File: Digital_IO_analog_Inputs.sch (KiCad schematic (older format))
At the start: 33 parts, among them J5 OSTTC020162, J7 OSTTC030162, J9 0022232031, Q3 BC817-25LT1G, Q4 BC817-25LT1G, U17 ISO1211DR, U24 ISO1211DR, U26 ISO1211DR

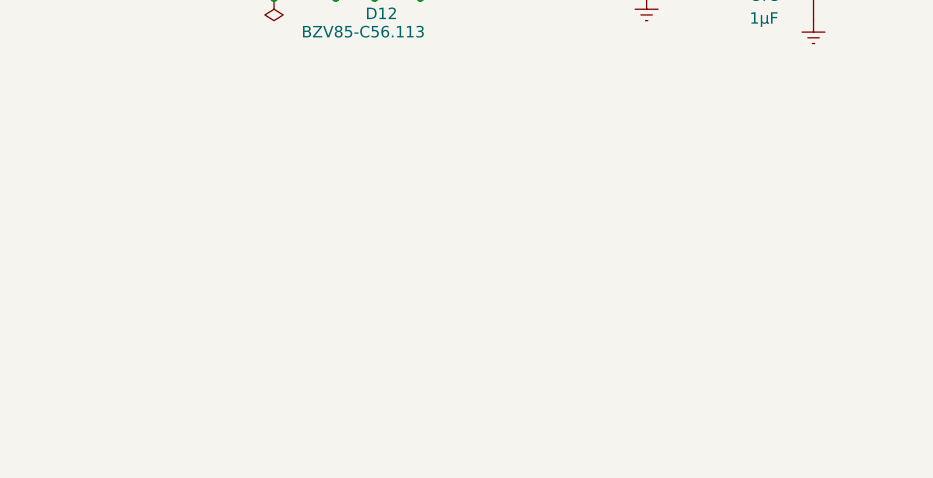
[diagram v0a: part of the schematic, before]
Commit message: Analog decoupling schema completed. Digital_IO completed and clean up
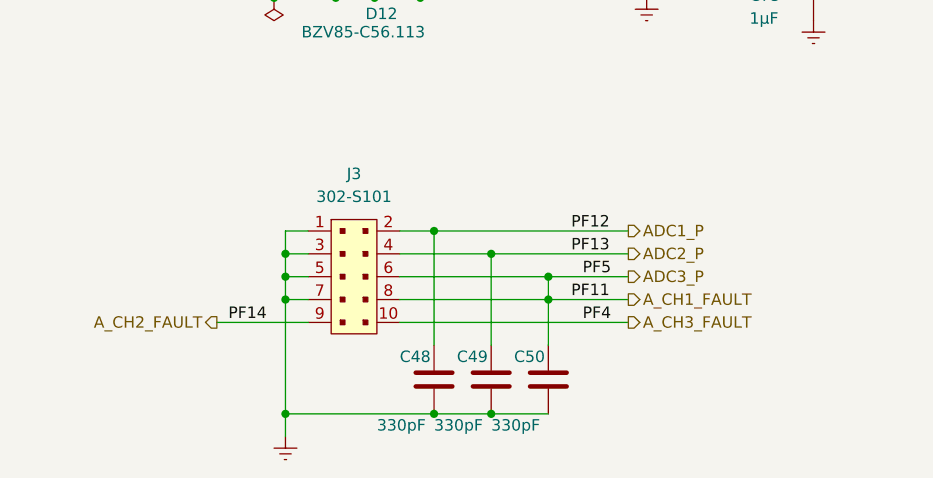
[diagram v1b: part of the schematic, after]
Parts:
- added C48, C49, C50: 330pF, Capacitor_SMD:C_0603_1608Metric_Pad1.08x0.95mm_HandSolder, symbol Device:C
- added J3: 302-S101, digikey-footprints:PinHeader_2x5_P2.54mm_Drill1.2mm, symbol dk_Rectangular-Connectors-Headers-Male-Pins:302-S101
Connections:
- net GNDREF: now also C48.2, C49.2, C50.2, J3.1, J3.3, J3.5, J3.7
- new net ADC1_P: C48.1, J3.2
- new net ADC2_P: C49.1, J3.4
- new net ADC3_P: C50.1, J3.6, J3.8
- new net A_CH2_FAULT: J3.9
- new net A_CH3_FAULT: J3.10
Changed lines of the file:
@@
 Wire Wire Line
 	7920 4280 7920 4410
+Text HLabel 3350 5450 2    50   Output ~ 0
+ADC1_P
+Text HLabel 3350 5750 2    50   Output ~ 0
+A_CH1_FAULT
+Text HLabel 3350 5550 2    50   Output ~ 0
+ADC2_P
+Text HLabel 1550 5850 0    50   Output ~ 0
+A_CH2_FAULT
+Text HLabel 3350 5650 2    50   Output ~ 0
+ADC3_P
+Text HLabel 3350 5850 2    50   Output ~ 0
+A_CH3_FAULT
+$Comp
+L dk_Rectangular-Connectors-Headers-Male-Pins:302-S101 J3
+U 1 1 60B0C96F
+P 2150 5650
+F 0 "J3" H 2150 6100 50  0000 C CNN
+F 1 "302-S101" H 2150 6000 50  0000 C CNN
+F 2 "digikey-footprints:PinHeader_2x5_P2.54mm_Drill1.2mm" H 2350 5850 60  0001 L CNN
+F 3 "http://www.on-shore.com/wp-content/uploads/2018/04/302-SXX1.pdf" V 2350 5950 60  0001 L CNN
+F 4 "ED1543-ND" H 2350 6050 60  0001 L CNN "Digi-Key_PN"
+F 5 "302-S101" H 2350 6150 60  0001 L CNN "MPN"
+F 6 "Connectors, Interconnects" H 2350 6250 60  0001 L CNN "Category"
+F 7 "Rectangular Connectors - Headers, Male Pins" H 2350 6350 60  0001 L CNN "Family"
+F 8 "http://www.on-shore.com/wp-content/uploads/2018/04/302-SXX1.pdf" H 2350 6450 60  0001 L CNN "DK_Datasheet_Link"
+F 9 "/product-detail/en/on-shore-technology-inc/302-S101/ED1543-ND/2178422" H 2350 6550 60  0001 L CNN "DK_Detail_Page"
+F 10 "CONN HEADER VERT 10POS 2.54MM" H 2350 6650 60  0001 L CNN "Description"
+F 11 "On Shore Technology Inc." H 2350 6750 60  0001 L CNN "Manufacturer"
+F 12 "Active" H 2350 6850 60  0001 L CNN "Status"
+	1    2150 5650
+	1    0    0    -1
+$EndComp
+Wire Wire Line
+	1950 5850 1550 5850
+Wire Wire Line
+	2350 5450 2500 5450
+Wire Wire Line
+	1950 5450 1850 5450
+Wire Wire Line
+	1850 5450 1850 5550
+Wire Wire Line
+	1950 5550 1850 5550
+Connection ~ 1850 5550
+Wire Wire Line
+	1850 5550 1850 5650
+Wire Wire Line
+	1950 5650 1850 5650
+Connection ~ 1850 5650
+Wire Wire Line
+	1850 5650 1850 5750
+Wire Wire Line
+	1950 5750 1850 5750
+Connection ~ 1850 5750
+Wire Wire Line
+	1850 5750 1850 6250
+$Comp
+L Device:C C?
+U 1 1 60B910A1
+P 2500 6100
+AR Path="/60B910A1" Ref="C?"  Part="1"
+AR Path="/60A03F8A/60B910A1" Ref="C?"  Part="1"
+AR Path="/60D8C564/60B910A1" Ref="C48"  Part="1"
+F 0 "C48" H 2350 6200 50  0000 L CNN
+F 1 "330pF" H 2250 5900 50  0000 L CNN
+F 2 "Capacitor_SMD:C_0603_1608Metric_Pad1.08x0.95mm_HandSolder" H 2538 5950 50  0001 C CNN
+F 3 "http://www.farnell.com/datasheets/2710676.pdf" H 2500 6100 50  0001 C CNN
+F 4 "GRM188R71H331KA01D" H 2500 6100 50  0001 C CNN "Type"
+	1    2500 6100
+	1    0    0    -1
+$EndComp
+Wire Wire Line
+	2500 5950 2500 5450
+$Comp
+L Device:C C?
+U 1 1 60B9DA68
+P 2750 6100
+AR Path="/60B9DA68" Ref="C?"  Part="1"
+AR Path="/60A03F8A/60B9DA68" Ref="C?"  Part="1"
+AR Path="/60D8C564/60B9DA68" Ref="C49"  Part="1"
+F 0 "C49" H 2600 6200 50  0000 L CNN
+F 1 "330pF" H 2500 5900 50  0000 L CNN
+F 2 "Capacitor_SMD:C_0603_1608Metric_Pad1.08x0.95mm_HandSolder" H 2788 5950 50  0001 C CNN
+F 3 "http://www.farnell.com/datasheets/2710676.pdf" H 2750 6100 50  0001 C CNN
+F 4 "GRM188R71H331KA01D" H 2750 6100 50  0001 C CNN "Type"
+	1    2750 6100
+	1    0    0    -1
+$EndComp
+$Comp
+L Device:C C?
+U 1 1 60B9DF75
+P 3000 6100
+AR Path="/60B9DF75" Ref="C?"  Part="1"
+AR Path="/60A03F8A/60B9DF75" Ref="C?"  Part="1"
+AR Path="/60D8C564/60B9DF75" Ref="C50"  Part="1"
+F 0 "C50" H 2850 6200 50  0000 L CNN
+F 1 "330pF" H 2750 5900 50  0000 L CNN
+F 2 "Capacitor_SMD:C_0603_1608Metric_Pad1.08x0.95mm_HandSolder" H 3038 5950 50  0001 C CNN
+F 3 "http://www.farnell.com/datasheets/2710676.pdf" H 3000 6100 50  0001 C CNN
+F 4 "GRM188R71H331KA01D" H 3000 6100 50  0001 C CNN "Type"
+	1    3000 6100
+	1    0    0    -1
+$EndComp
+Wire Wire Line
+	2750 5950 2750 5550
+Wire Wire Line
+	2750 5550 2350 5550
+Wire Wire Line
+	3000 5950 3000 5750
+Wire Wire Line
+	2350 5650 3000 5650
+Wire Wire Line
+	3000 5650 3350 5650
+Wire Wire Line
+	2350 5750 3000 5750
+Wire Wire Line
+	2350 5850 3350 5850
+Wire Wire Line
+	2750 5550 3350 5550
+Wire Wire Line
+	2500 5450 3350 5450
+$Comp
+L power:GNDREF #PWR?
+U 1 1 60BCDF96
+P 1850 6350
+AR Path="/60BCDF96" Ref="#PWR?"  Part="1"
+AR Path="/60A03F8A/60BCDF96" Ref="#PWR?"  Part="1"
+AR Path="/60D8C564/60BCDF96" Ref="#PWR0103"  Part="1"
+F 0 "#PWR0103" H 1850 6100 50  0001 C CNN
+F 1 "GNDREF" V 1855 6222 50  0001 R CNN
+F 2 "" H 1850 6350 50  0001 C CNN
+F 3 "" H 1850 6350 50  0001 C CNN
+	1    1850 6350
+	1    0    0    -1
+$EndComp
+Wire Wire Line
+	1850 6250 2500 6250
+Connection ~ 1850 6250
+Wire Wire Line
+	1850 6250 1850 6350
+Connection ~ 2500 6250
+Wire Wire Line
+	2500 6250 2750 6250
+Connection ~ 2750 6250
+Wire Wire Line
+	2750 6250 3000 6250
+Text Label 3150 5650 0    50   ~ 0
+PF5
+Text Label 3150 5850 0    50   ~ 0
+PF4
+Text Label 3100 5550 0    50   ~ 0
+PF13
+Text Label 1600 5850 0    50   ~ 0
+PF14
+Text Label 3100 5450 0    50   ~ 0
+PF12
+Text Label 3100 5750 0    50   ~ 0
+PF11
+Connection ~ 3000 5750
+Wire Wire Line
+	3000 5750 3000 5650
+Wire Wire Line
+	3000 5750 3350 5750
+Connection ~ 2500 5450
+Connection ~ 2750 5550
+Connection ~ 3000 5650
 $EndSCHEMATC

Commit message: main PCB changes
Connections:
- net ADC3_P: no longer J3.8
- new net A_CH1_FAULT: J3.8
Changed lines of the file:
@@
 	2750 5550 2350 5550
-Wire Wire Line
-	3000 5950 3000 5750
-Wire Wire Line
-	2350 5650 3000 5650
-Wire Wire Line
-	3000 5650 3350 5650
-Wire Wire Line
-	2350 5750 3000 5750
 Wire Wire Line
 	2350 5850 3350 5850
@@
 Text Label 3100 5750 0    50   ~ 0
 PF11
-Connection ~ 3000 5750
-Wire Wire Line
-	3000 5750 3000 5650
-Wire Wire Line
-	3000 5750 3350 5750
 Connection ~ 2500 5450
 Connection ~ 2750 5550
+Wire Wire Line
+	2350 5650 3000 5650
+Wire Wire Line
+	2350 5750 3350 5750
+Wire Wire Line
+	3000 5650 3000 5950
 Connection ~ 3000 5650
+Wire Wire Line
+	3000 5650 3350 5650
 $EndSCHEMATC

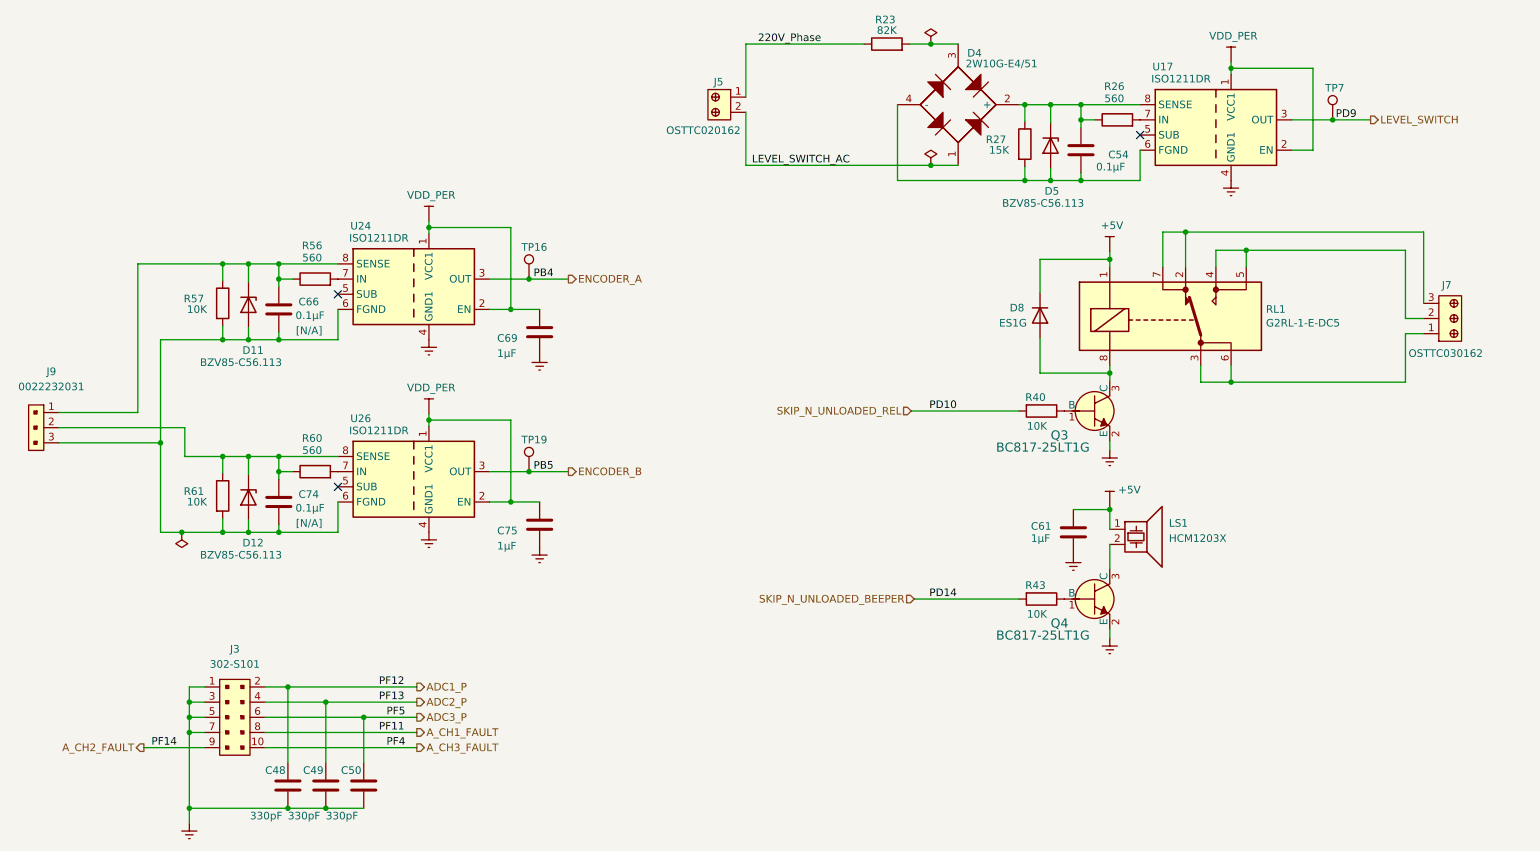
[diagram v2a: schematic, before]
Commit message: LAN elements placed
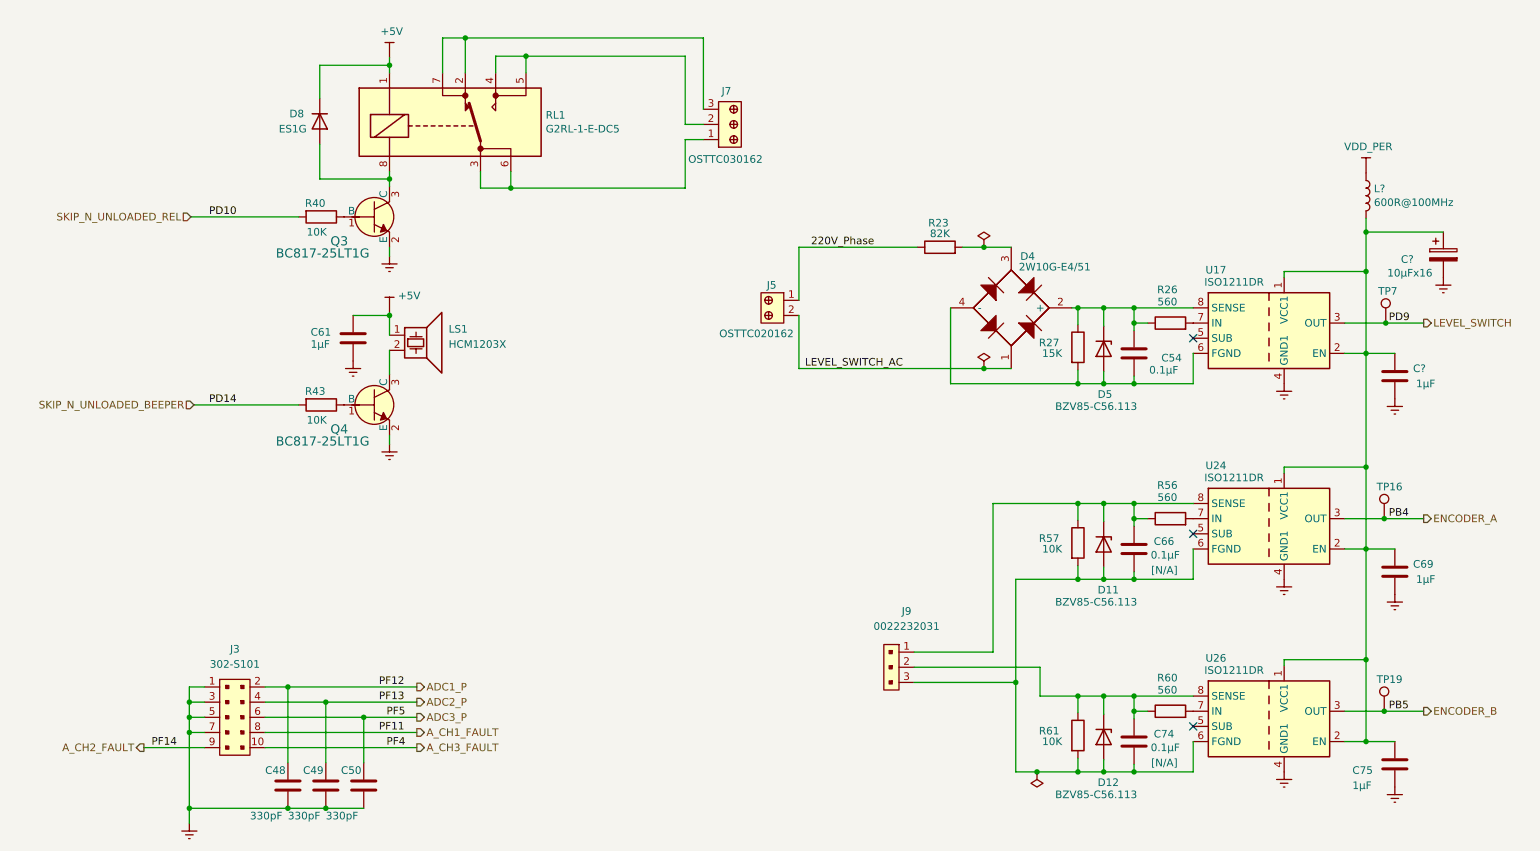
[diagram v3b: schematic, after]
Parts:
- added C?: 1µF, Capacitor_SMD:C_0603_1608Metric_Pad1.08x0.95mm_HandSolder, symbol Device:C
- added C?: 10µFx16, Capacitor_Tantalum_SMD:CP_EIA-3216-10_Kemet-I, symbol Device:CP
- added L?: 600R@100MHz, Inductor_SMD:L_0805_2012Metric_Pad1.15x1.40mm_HandSolder, symbol Device:L
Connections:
- net GNDREF: now also C?.2, C?.2
- net VDD_PER: now also L?.1; no longer C69.1, C75.1, U17.1 (VCC1), U17.2 (EN), U24.1 (VCC1), U24.2 (EN), U26.1 (VCC1), U26.2 (EN)
- new net: C69.1, C75.1, C?.1, C?.1, L?.2, U17.1 (VCC1), U17.2 (EN), U24.1 (VCC1), U24.2 (EN), U26.1 (VCC1), U26.2 (EN)
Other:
- moved on the sheet: C54, C61, C66, C69, C74, C75, D11, D12, D4, D5, D8, J5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

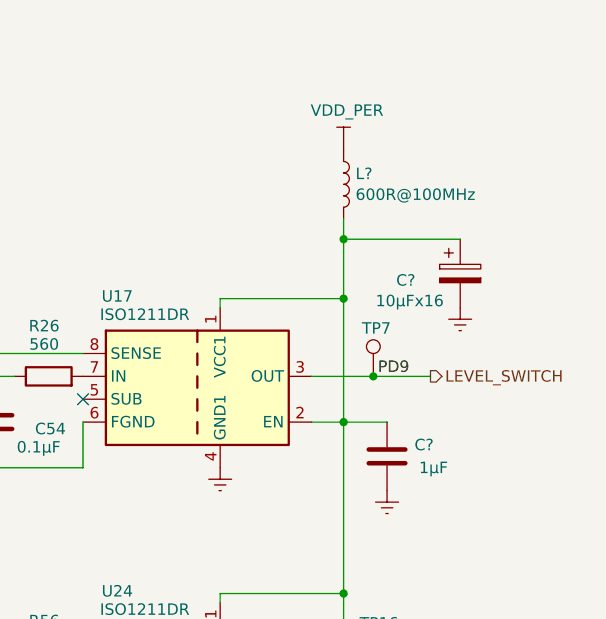
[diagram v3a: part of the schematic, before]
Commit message: ISO1211 power supply apdated. Label USB_GND added
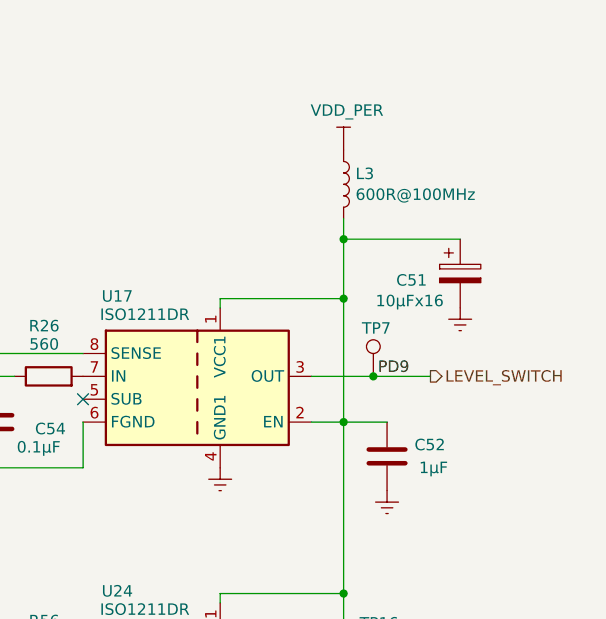
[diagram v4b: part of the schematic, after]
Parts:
- gave numbers to parts that had none: 3
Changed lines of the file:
@@
 AR Path="/60A03F8A/60C75DBE" Ref="L?"  Part="1"
 AR Path="/608C7842/60C75DBE" Ref="L?"  Part="1"
-AR Path="/60D8C564/60C75DBE" Ref="L?"  Part="1"
-F 0 "L?" H 9662 2256 50  0000 L CNN
+AR Path="/60D8C564/60C75DBE" Ref="L3"  Part="1"
+F 0 "L3" H 9662 2256 50  0000 L CNN
 F 1 "600R@100MHz" H 9662 2165 50  0000 L CNN
 F 2 "Inductor_SMD:L_0805_2012Metric_Pad1.15x1.40mm_HandSolder" H 9610 2210 50  0001 C CNN
@@
 $EndComp
 $Comp
-L SVIELCOM_Library:VDD_PER #PWR?
+L SVIELCOM_Library:VDD_PER #PWR0104
 U 1 1 60C7C9BC
 P 9610 2060
-F 0 "#PWR?" H 9610 1910 50  0001 C CNN
+F 0 "#PWR0104" H 9610 1910 50  0001 C CNN
 F 1 "VDD_PER" H 9625 2233 50  0000 C CNN
 F 2 "" H 9610 2060 50  0001 C CNN
@@
 AR Path="/60CE730E" Ref="C?"  Part="1"
 AR Path="/60A03F8A/60CE730E" Ref="C?"  Part="1"
-AR Path="/60D8C564/60CE730E" Ref="C?"  Part="1"
-F 0 "C?" H 9920 3450 50  0000 L CNN
+AR Path="/60D8C564/60CE730E" Ref="C52"  Part="1"
+F 0 "C52" H 9920 3450 50  0000 L CNN
 F 1 "1µF" H 9940 3350 50  0000 L CNN
 F 2 "Capacitor_SMD:C_0603_1608Metric_Pad1.08x0.95mm_HandSolder" H 9838 3250 50  0001 C CNN
@@
 AR Path="/60CE7314" Ref="#PWR?"  Part="1"
 AR Path="/60A03F8A/60CE7314" Ref="#PWR?"  Part="1"
-AR Path="/60D8C564/60CE7314" Ref="#PWR?"  Part="1"
-F 0 "#PWR?" H 9800 3300 50  0001 C CNN
+AR Path="/60D8C564/60CE7314" Ref="#PWR0105"  Part="1"
+F 0 "#PWR0105" H 9800 3300 50  0001 C CNN
 F 1 "GNDREF" V 9805 3422 50  0001 R CNN
 F 2 "" H 9800 3550 50  0001 C CNN
@@
 AR Path="/60CFD521" Ref="C?"  Part="1"
 AR Path="/60A03F8A/60CFD521" Ref="C?"  Part="1"
-F 0 "C?" H 9840 2570 50  0000 L CNN
+AR Path="/60D8C564/60CFD521" Ref="C51"  Part="1"
+F 0 "C51" H 9840 2570 50  0000 L CNN
 F 1 "10µFx16" H 9750 2480 50  0000 L CNN
 F 2 "Capacitor_Tantalum_SMD:CP_EIA-3216-10_Kemet-I" H 10158 2450 50  0001 C CNN
@@
 AR Path="/60D09CB9" Ref="#PWR?"  Part="1"
 AR Path="/60A03F8A/60D09CB9" Ref="#PWR?"  Part="1"
-AR Path="/60D8C564/60D09CB9" Ref="#PWR?"  Part="1"
-F 0 "#PWR?" H 10120 2500 50  0001 C CNN
+AR Path="/60D8C564/60D09CB9" Ref="#PWR0106"  Part="1"
+F 0 "#PWR0106" H 10120 2500 50  0001 C CNN
 F 1 "GNDREF" V 10125 2622 50  0001 R CNN
 F 2 "" H 10120 2750 50  0001 C CNN

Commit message: PCB layout
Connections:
- net COM_ENCODER: now reaches C66.2, C74.2, D11.2 (A), D12.2 (A), J9.3, R57.2, R61.2, U24.6 (FGND), U26.6 (FGND)
- net ENCODER_IN_A: now reaches C66.1, D11.1 (K), J9.1, R56.1, R57.1, U24.8 (SENSE)
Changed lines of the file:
@@
 Wire Wire Line
 	2750 6250 3000 6250
-Text Label 3150 5650 0    50   ~ 0
-PF5
-Text Label 3150 5850 0    50   ~ 0
+Text Label 3090 5650 0    50   ~ 0
+PC3_C
+Text Label 3110 5850 0    50   ~ 0
 PF4
 Text Label 3100 5550 0    50   ~ 0
@@
 	1    0    0    -1
 $EndComp
+Text Label 7210 5420 2    50   ~ 0
+COM_ENCODER
+Text Label 7150 4340 3    50   ~ 0
+ENCODER_IN_A
+Text Label 7300 4740 3    50   ~ 0
+ENCODER_IN_B
 $EndSCHEMATC

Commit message: PCB minor changes
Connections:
- net ENCODER_IN_B: now reaches C74.1, D12.1 (K), J9.2, R60.1, R61.1, U26.8 (SENSE)
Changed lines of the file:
@@
 U 1 1 6139B5AD
 P 6530 5220
-F 0 "J9" V 6260 5270 50  0000 C CNN
-F 1 "0022232031" V 6360 5270 50  0000 C CNN
+F 0 "J9" V 6420 5170 50  0000 C CNN
+F 1 "0022232031" V 6360 5270 50  0001 C CNN
 F 2 "digikey-footprints:PinHeader_1x3_P2.54mm_Drill1.02mm" H 6730 5420 60  0001 L CNN
 F 3 "https://www.molex.com/pdm_docs/sd/022232031_sd.pdf" H 6730 5520 60  0001 L CNN
@@
 Text Label 7150 4340 3    50   ~ 0
 ENCODER_IN_A
-Text Label 7300 4740 3    50   ~ 0
+Text Label 6654 5320 0    50   ~ 0
 ENCODER_IN_B
 $EndSCHEMATC

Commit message: PCB before Gerber creating
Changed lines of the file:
@@
 	2930 3000 3170 3000
 Text Label 1980 2350 0    50   ~ 0
-PD10
+PE0
 Text Label 1980 3590 0    50   ~ 0
-PD14
+PE1
 Text Label 9760 3050 0    50   ~ 0
-PD9
+PA15
 $Comp
 L dk_Terminal-Blocks-Wire-to-Board:OSTTC020162 J5
@@
 PC3_C
 Text Label 3110 5850 0    50   ~ 0
-PF4
+PB15
 Text Label 3100 5550 0    50   ~ 0
 PF13
 Text Label 1600 5850 0    50   ~ 0
-PF14
+PB14
 Text Label 3100 5450 0    50   ~ 0
 PF12
 Text Label 3100 5750 0    50   ~ 0
-PF11
+PD8
 Connection ~ 2500 5450
 Connection ~ 2750 5550

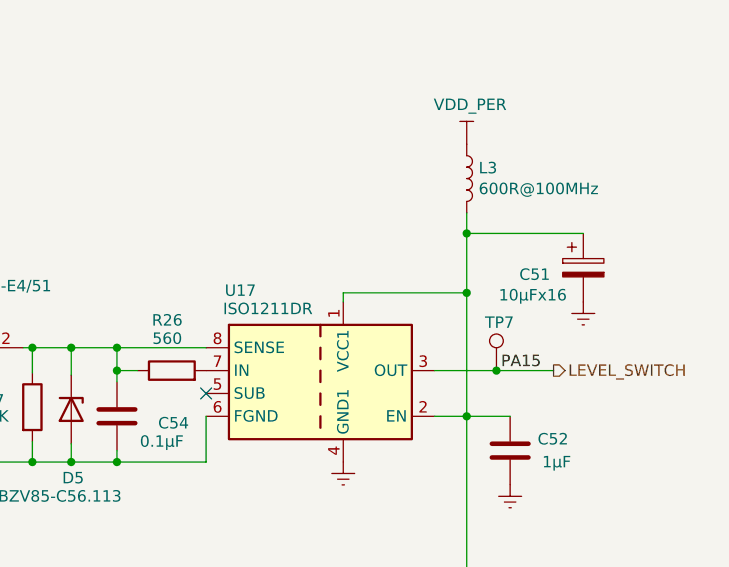
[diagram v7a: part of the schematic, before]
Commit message: minor changes and add NRST to J16
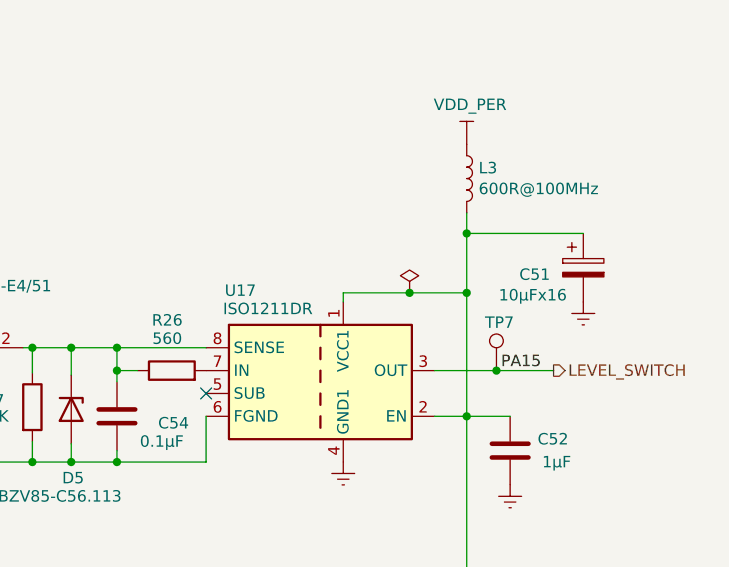
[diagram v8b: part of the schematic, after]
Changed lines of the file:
@@
 	9070 2750 9070 2710
 Wire Wire Line
-	9070 2710 9610 2710
+	9070 2710 9360 2710
 Wire Wire Line
 	9610 2710 9610 3250
@@
 Text Label 6654 5320 0    50   ~ 0
 ENCODER_IN_B
+$Comp
+L power:PWR_FLAG #FLG0102
+U 1 1 60C68E0F
+P 9360 2710
+F 0 "#FLG0102" H 9360 2785 50  0001 C CNN
+F 1 "PWR_FLAG" H 9370 2900 50  0001 C CNN
+F 2 "" H 9360 2710 50  0001 C CNN
+F 3 "~" H 9360 2710 50  0001 C CNN
+	1    9360 2710
+	1    0    0    -1
+$EndComp
+Connection ~ 9360 2710
+Wire Wire Line
+	9360 2710 9610 2710
 $EndSCHEMATC
